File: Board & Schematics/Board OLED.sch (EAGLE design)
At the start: 20 parts

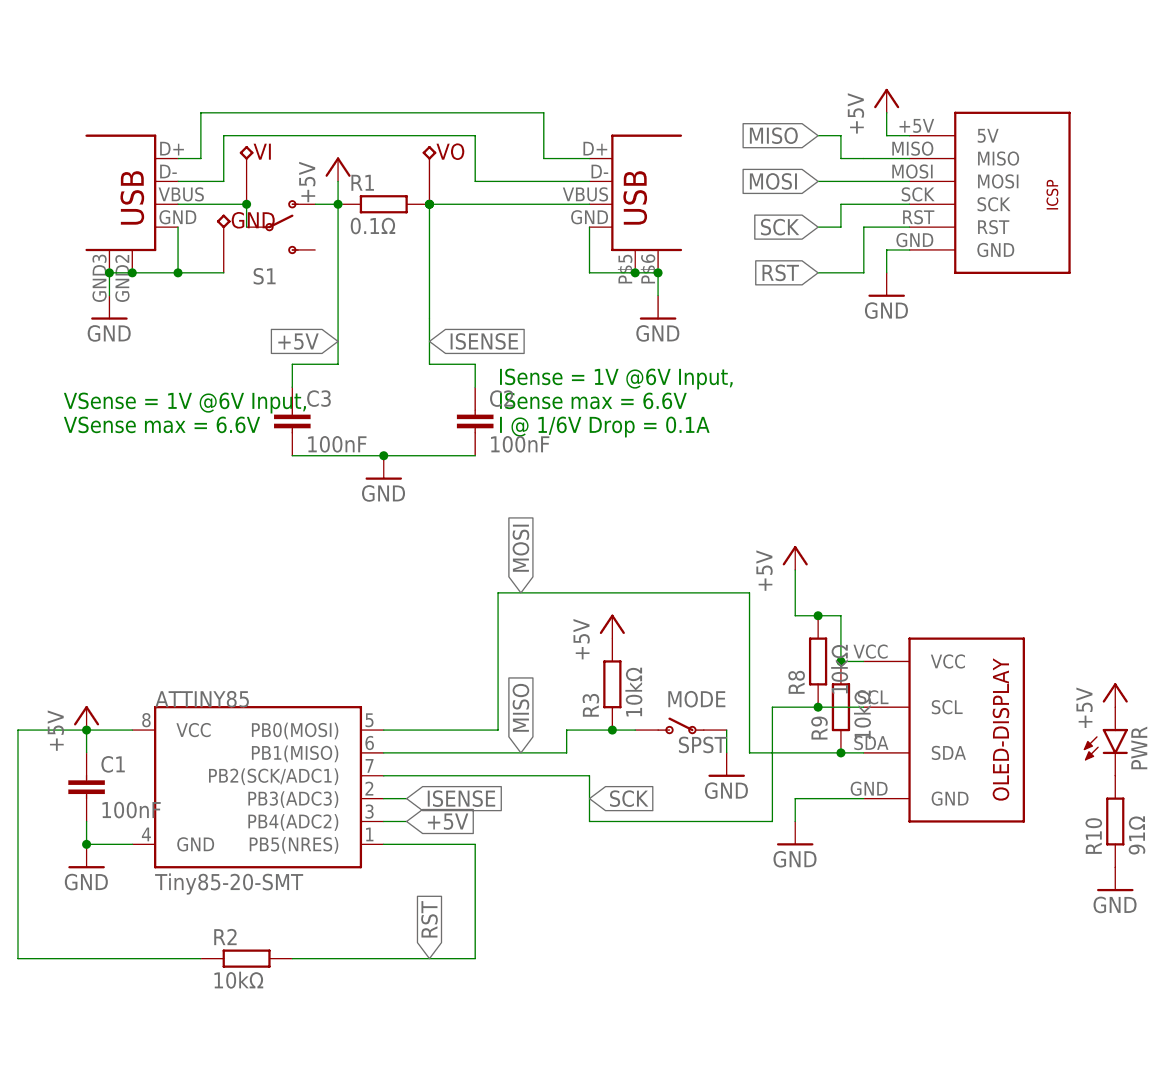
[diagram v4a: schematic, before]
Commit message: added attenuation resistor network to mode switch pin
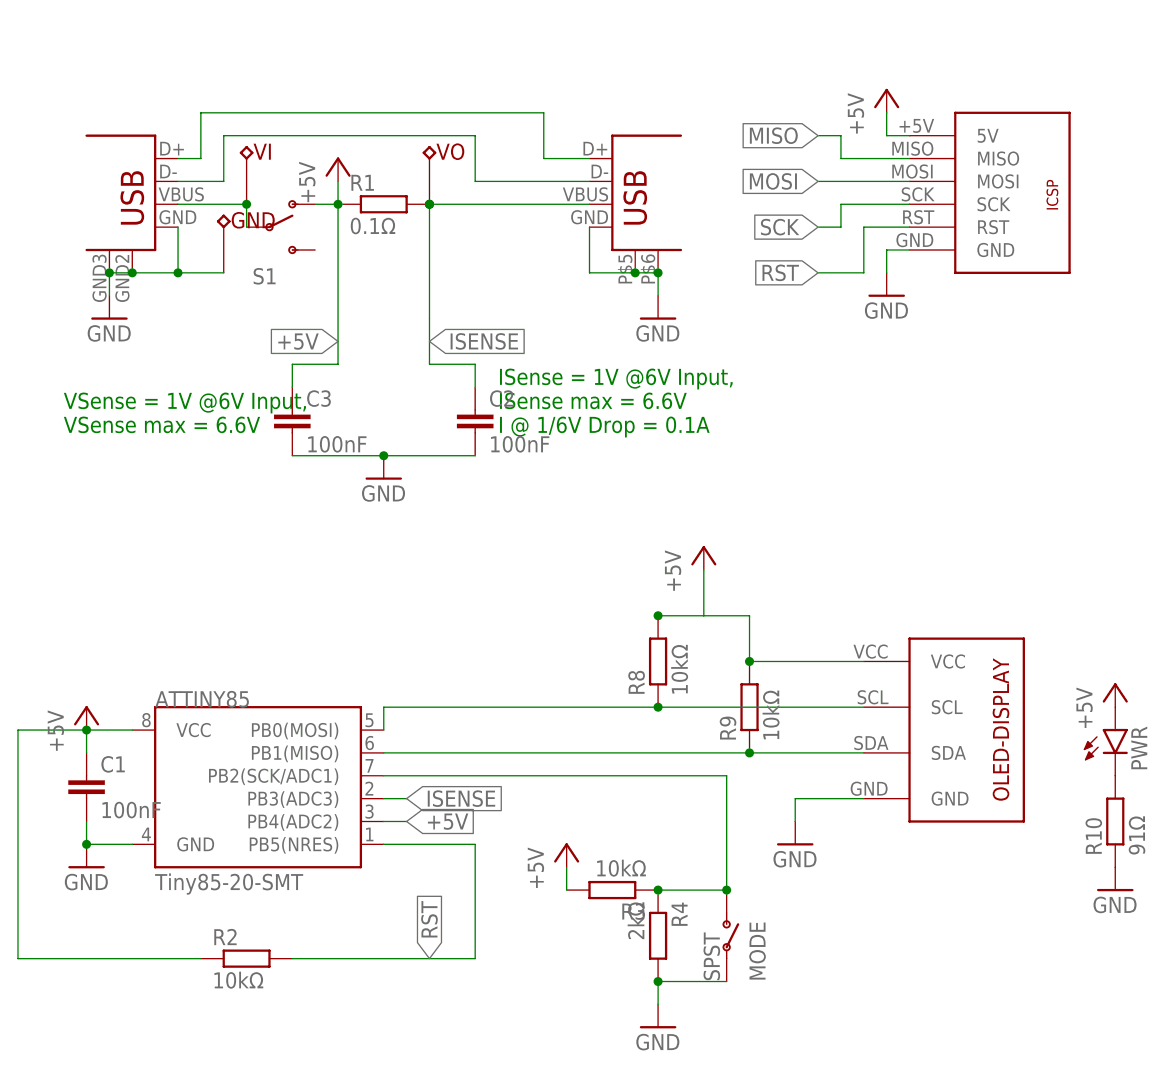
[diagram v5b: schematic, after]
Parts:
- added R4: 2kΩ, rcl:R-EU_R0603
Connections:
- net GND: now also R4.2
- net MISO: now also R9.1, U$2.SDA; no longer MODE.O, R3.1
- net MOSI: now also R8.1, U$2.SCL; no longer R9.1, U$2.SDA
- net SCK: now also MODE.O, R3.1, R4.1; no longer R8.1, U$2.SCL
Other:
- moved on the sheet: MODE, R3, R8, R9
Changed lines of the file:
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@@
 <part name="GND4" library="SparkFun-Aesthetics" deviceset="GND" device=""/>
 <part name="MODE" library="OwnStuff" deviceset="SPST" device="" value="SPST"/>
-<part name="GND5" library="SparkFun-Aesthetics" deviceset="GND" device=""/>
 <part name="P+4" library="supply1" deviceset="+5V" device=""/>
 <part name="R3" library="rcl" deviceset="R-EU_" device="R0603" value="10kΩ"/>
@@
 <part name="R10" library="rcl" deviceset="R-EU_" device="R0603" value="91Ω"/>
 <part name="GND" library="OwnStuff" deviceset="TESTPOINT" device="0.5MM-DRILL-WIRE-LOOP"/>
+<part name="R4" library="rcl" deviceset="R-EU_" device="R0603" value="2kΩ"/>
+<part name="GND5" library="SparkFun-Aesthetics" deviceset="GND" device=""/>
 </parts>
 <sheets>
@@
 <instance part="OUTPUT" gate="G$1" x="60.96" y="55.88"/>
 <instance part="GND3" gate="1" x="66.04" y="45.72"/>
-<instance part="P+3" gate="1" x="81.28" y="20.32"/>
+<instance part="P+3" gate="1" x="71.12" y="20.32"/>
 <instance part="GND4" gate="1" x="81.28" y="-12.7"/>
-<instance part="MODE" gate="G$1" x="68.58" y="0" rot="MR0"/>
-<instance part="GND5" gate="1" x="73.66" y="-5.08"/>
-<instance part="P+4" gate="1" x="60.96" y="12.7"/>
-<instance part="R3" gate="G$1" x="60.96" y="5.08" rot="R90"/>
+<instance part="MODE" gate="G$1" x="73.66" y="-22.86" rot="MR90"/>
+<instance part="P+4" gate="1" x="55.88" y="-12.7"/>
+<instance part="R3" gate="G$1" x="60.96" y="-17.78" rot="R180"/>
 <instance part="U$1" gate="G$1" x="104.14" y="58.42"/>
 <instance part="P+5" gate="1" x="91.44" y="71.12"/>
@@
 <instance part="C3" gate="G$1" x="25.4" y="35.56"/>
 <instance part="U$2" gate="G$1" x="96.52" y="0"/>
-<instance part="R8" gate="G$1" x="83.82" y="7.62" rot="R90"/>
-<instance part="R9" gate="G$1" x="86.36" y="2.54" rot="R90"/>
+<instance part="R8" gate="G$1" x="66.04" y="7.62" rot="R90"/>
+<instance part="R9" gate="G$1" x="76.2" y="2.54" rot="R90"/>
 <instance part="VI" gate="G$1" x="20.32" y="58.42"/>
 <instance part="VO" gate="G$1" x="40.64" y="58.42"/>
@@
 <instance part="R10" gate="G$1" x="116.84" y="-10.16" rot="R90"/>
 <instance part="GND" gate="G$1" x="17.78" y="50.8"/>
+<instance part="R4" gate="G$1" x="66.04" y="-22.86" rot="R270"/>
+<instance part="GND5" gate="1" x="66.04" y="-33.02"/>
 </instances>
 <busses>
@@
 </segment>
 <segment>
-<pinref part="MODE" gate="G$1" pin="P"/>
-<pinref part="GND5" gate="1" pin="GND"/>
-<wire x1="73.66" y1="0" x2="73.66" y2="-2.54" width="0.1524" layer="91"/>
-</segment>
-<segment>
 <pinref part="OUTPUT" gate="G$1" pin="GND"/>
 <wire x1="58.42" y1="50.8" x2="58.42" y2="55.88" width="0.1524" layer="91"/>
@@
 <pinref part="R10" gate="G$1" pin="1"/>
 <pinref part="GND7" gate="1" pin="GND"/>
+</segment>
+<segment>
+<pinref part="R4" gate="G$1" pin="2"/>
+<pinref part="GND5" gate="1" pin="GND"/>
+<wire x1="66.04" y1="-30.48" x2="66.04" y2="-27.94" width="0.1524" layer="91"/>
+<pinref part="MODE" gate="G$1" pin="P"/>
+<wire x1="73.66" y1="-27.94" x2="66.04" y2="-27.94" width="0.1524" layer="91"/>
+<junction x="66.04" y="-27.94"/>
 </segment>
 </net>
@@
 <pinref part="P+3" gate="1" pin="+5V"/>
 <pinref part="U$2" gate="G$1" pin="VCC"/>
-<wire x1="81.28" y1="12.7" x2="81.28" y2="17.78" width="0.1524" layer="91"/>
-<wire x1="88.9" y1="7.62" x2="86.36" y2="7.62" width="0.1524" layer="91"/>
+<wire x1="71.12" y1="12.7" x2="71.12" y2="17.78" width="0.1524" layer="91"/>
+<wire x1="88.9" y1="7.62" x2="76.2" y2="7.62" width="0.1524" layer="91"/>
 <pinref part="R9" gate="G$1" pin="2"/>
-<wire x1="86.36" y1="7.62" x2="86.36" y2="12.7" width="0.1524" layer="91"/>
-<junction x="86.36" y="7.62"/>
+<wire x1="76.2" y1="7.62" x2="76.2" y2="12.7" width="0.1524" layer="91"/>
+<junction x="76.2" y="7.62"/>
 <pinref part="R8" gate="G$1" pin="2"/>
-<wire x1="86.36" y1="12.7" x2="83.82" y2="12.7" width="0.1524" layer="91"/>
-<wire x1="83.82" y1="12.7" x2="81.28" y2="12.7" width="0.1524" layer="91"/>
-<junction x="83.82" y="12.7"/>
+<wire x1="66.04" y1="12.7" x2="71.12" y2="12.7" width="0.1524" layer="91"/>
+<junction x="66.04" y="12.7"/>
+<wire x1="76.2" y1="12.7" x2="71.12" y2="12.7" width="0.1524" layer="91"/>
 </segment>
 <segment>
@@
 <wire x1="93.98" y1="66.04" x2="91.44" y2="66.04" width="0.1524" layer="91"/>
 <wire x1="91.44" y1="66.04" x2="91.44" y2="68.58" width="0.1524" layer="91"/>
-</segment>
-<segment>
-<pinref part="R3" gate="G$1" pin="2"/>
-<pinref part="P+4" gate="1" pin="+5V"/>
 </segment>
 <segment>
@@
 <label x="38.1" y="-10.16" size="1.778" layer="95" xref="yes"/>
 </segment>
+<segment>
+<pinref part="R3" gate="G$1" pin="2"/>
+<pinref part="P+4" gate="1" pin="+5V"/>
+<wire x1="55.88" y1="-17.78" x2="55.88" y2="-15.24" width="0.1524" layer="91"/>
+</segment>
 </net>
 <net name="RST" class="0">
@@
 <net name="MOSI" class="0">
 <segment>
-<pinref part="ATTINY85" gate="G$1" pin="PB0(MOSI)"/>
-<wire x1="48.26" y1="0" x2="35.56" y2="0" width="0.1524" layer="91"/>
-<wire x1="48.26" y1="0" x2="48.26" y2="15.24" width="0.1524" layer="91"/>
-<wire x1="76.2" y1="-2.54" x2="76.2" y2="15.24" width="0.1524" layer="91"/>
-<wire x1="76.2" y1="15.24" x2="48.26" y2="15.24" width="0.1524" layer="91"/>
-<label x="50.8" y="15.24" size="1.778" layer="95" rot="R90" xref="yes"/>
-<pinref part="U$2" gate="G$1" pin="SDA"/>
-<wire x1="86.36" y1="-2.54" x2="88.9" y2="-2.54" width="0.1524" layer="91"/>
-<pinref part="R9" gate="G$1" pin="1"/>
-<wire x1="76.2" y1="-2.54" x2="86.36" y2="-2.54" width="0.1524" layer="91"/>
-<junction x="86.36" y="-2.54"/>
-</segment>
-<segment>
 <pinref part="U$1" gate="G$1" pin="MOSI"/>
 <wire x1="93.98" y1="60.96" x2="83.82" y2="60.96" width="0.1524" layer="91"/>
 <label x="83.82" y="60.96" size="1.778" layer="95" rot="R180" xref="yes"/>
 </segment>
+<segment>
+<pinref part="U$2" gate="G$1" pin="SCL"/>
+<wire x1="88.9" y1="2.54" x2="66.04" y2="2.54" width="0.1524" layer="91"/>
+<pinref part="R8" gate="G$1" pin="1"/>
+<junction x="66.04" y="2.54"/>
+<pinref part="ATTINY85" gate="G$1" pin="PB0(MOSI)"/>
+<wire x1="66.04" y1="2.54" x2="35.56" y2="2.54" width="0.1524" layer="91"/>
+<wire x1="35.56" y1="2.54" x2="35.56" y2="0" width="0.1524" layer="91"/>
+</segment>
 </net>
 <net name="SCK" class="0">
-<segment>
-<wire x1="58.42" y1="-10.16" x2="78.74" y2="-10.16" width="0.1524" layer="91"/>
-<wire x1="78.74" y1="-10.16" x2="78.74" y2="2.54" width="0.1524" layer="91"/>
-<label x="58.42" y="-7.62" size="1.778" layer="95" xref="yes"/>
-<pinref part="ATTINY85" gate="G$1" pin="PB2(SCK/ADC1)"/>
-<wire x1="35.56" y1="-5.08" x2="58.42" y2="-5.08" width="0.1524" layer="91"/>
-<wire x1="58.42" y1="-10.16" x2="58.42" y2="-5.08" width="0.1524" layer="91"/>
-<pinref part="U$2" gate="G$1" pin="SCL"/>
-<wire x1="88.9" y1="2.54" x2="83.82" y2="2.54" width="0.1524" layer="91"/>
-<pinref part="R8" gate="G$1" pin="1"/>
-<wire x1="78.74" y1="2.54" x2="83.82" y2="2.54" width="0.1524" layer="91"/>
-<junction x="83.82" y="2.54"/>
-</segment>
 <segment>
 <pinref part="U$1" gate="G$1" pin="SCK"/>
@@
 <wire x1="86.36" y1="55.88" x2="83.82" y2="55.88" width="0.1524" layer="91"/>
 <label x="83.82" y="55.88" size="1.778" layer="95" rot="R180" xref="yes"/>
+</segment>
+<segment>
+<pinref part="R3" gate="G$1" pin="1"/>
+<pinref part="MODE" gate="G$1" pin="O"/>
+<wire x1="66.04" y1="-17.78" x2="73.66" y2="-17.78" width="0.1524" layer="91"/>
+<wire x1="73.66" y1="-17.78" x2="73.66" y2="-5.08" width="0.1524" layer="91"/>
+<junction x="73.66" y="-17.78"/>
+<pinref part="ATTINY85" gate="G$1" pin="PB2(SCK/ADC1)"/>
+<wire x1="73.66" y1="-5.08" x2="35.56" y2="-5.08" width="0.1524" layer="91"/>
+<pinref part="R4" gate="G$1" pin="1"/>
+<junction x="66.04" y="-17.78"/>
 </segment>
 </net>
@@
 </segment>
 <segment>
+<wire x1="76.2" y1="-2.54" x2="35.56" y2="-2.54" width="0.1524" layer="91"/>
+<pinref part="U$2" gate="G$1" pin="SDA"/>
+<wire x1="76.2" y1="-2.54" x2="88.9" y2="-2.54" width="0.1524" layer="91"/>
+<pinref part="R9" gate="G$1" pin="1"/>
+<junction x="76.2" y="-2.54"/>
 <pinref part="ATTINY85" gate="G$1" pin="PB1(MISO)"/>
-<wire x1="55.88" y1="0" x2="55.88" y2="-2.54" width="0.1524" layer="91"/>
-<wire x1="55.88" y1="-2.54" x2="35.56" y2="-2.54" width="0.1524" layer="91"/>
-<label x="50.8" y="-2.54" size="1.778" layer="95" rot="R90" xref="yes"/>
-<pinref part="R3" gate="G$1" pin="1"/>
-<wire x1="55.88" y1="0" x2="60.96" y2="0" width="0.1524" layer="91"/>
-<pinref part="MODE" gate="G$1" pin="O"/>
-<wire x1="60.96" y1="0" x2="63.5" y2="0" width="0.1524" layer="91"/>
-<junction x="60.96" y="0"/>
-</segment>
-</net>
+</segment>
+</net>
